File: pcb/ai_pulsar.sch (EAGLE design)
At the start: 24 parts, among them IC1 DS1307SO8-TIGHT, IC3 74HCT245MTC, J2 1X05, U1 MIC5205-3.3

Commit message: routing finished
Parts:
- 3V-BATT: value (none) -> CR1220
- D1: value (none) -> PMEG2010AEB; device Ai_DiscreteSemis:DIODE-SCHOTTKYSMA-403D -> Ai_DiscreteSemis:DIODE-SCHOTTKYSOD-523
- J1: value (none) -> JST-3-MALE
- XL1: value (none) -> CMR200T
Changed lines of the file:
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@@
 <part name="U$7" library="Ai_Power" deviceset="5V" device=""/>
 <part name="U$11" library="Ai_Power" deviceset="5V" device=""/>
-<part name="3V-BATT" library="Ai_Connectors" deviceset="CR1220" device="SMT"/>
+<part name="3V-BATT" library="Ai_Connectors" deviceset="CR1220" device="SMT" value="CR1220"/>
 <part name="IC1" library="Ai_IC" deviceset="DS1307" device="SO8-TIGHT"/>
-<part name="J1" library="Ai_Connectors" deviceset="JST-3-MALE" device=""/>
+<part name="J1" library="Ai_Connectors" deviceset="JST-3-MALE" device="" value=""/>
 <part name="-" library="Ai_Connectors" deviceset="1X01-PETAL" device=""/>
 <part name="+" library="Ai_Connectors" deviceset="1X01-PETAL" device=""/>
@@
 <part name="R3" library="Ai_Passives" deviceset="RES" device="0603" value="10K"/>
 <part name="U$2" library="Ai_Power" deviceset="5V" device=""/>
-<part name="XL1" library="Ai_FrequencyControl" deviceset="CRYSTAL" device="CYL-2X6MM-SMT"/>
+<part name="XL1" library="Ai_FrequencyControl" deviceset="CRYSTAL" device="CYL-2X6MM-SMT" value="CMR200T"/>
 <part name="U$3" library="Ai_Power" deviceset="3V3" device=""/>
-<part name="D1" library="Ai_DiscreteSemis" deviceset="DIODE-SCHOTTKY" device="SMA-403D"/>
+<part name="D1" library="Ai_DiscreteSemis" deviceset="DIODE-SCHOTTKY" device="SOD-523" value="PMEG2010AEB"/>
 </parts>
 <sheets>
@@
 </sheet>
 </sheets>
+<errors>
+</errors>
 </schematic>
 </drawing>

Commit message: renamed a few parts
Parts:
- C1: value 0.01uF -> 0.1uF
- renumbered IC3 to IC2
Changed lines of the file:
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@@
 <?xml version="1.0" encoding="utf-8"?>
 <!DOCTYPE eagle SYSTEM "eagle.dtd">
-<eagle version="7.1.0">
+<eagle version="7.0.0">
 <drawing>
 <settings>
@@
 <setting verticaltext="up"/>
 </settings>
-<grid distance="50" unitdist="mil" unit="mil" style="lines" multiple="1" display="yes" altdistance="0.01" altunitdist="inch" altunit="inch"/>
+<grid distance="0.1" unitdist="inch" unit="inch" style="lines" multiple="1" display="no" altdistance="0.01" altunitdist="inch" altunit="inch"/>
 <layers>
 <layer number="1" name="Top" color="4" fill="1" visible="no" active="no"/>
@@
 <part name="R1" library="Ai_Passives" deviceset="RES" device="0603" value="1K"/>
 <part name="R2" library="Ai_Passives" deviceset="RES" device="0603" value="1K"/>
-<part name="C1" library="Ai_Passives" deviceset="CAP" device="0603" value="0.01uF"/>
+<part name="C1" library="Ai_Passives" deviceset="CAP" device="0603" value="0.1uF"/>
 <part name="GND5" library="Ai_Power" deviceset="GND" device=""/>
 <part name="U$1" library="Ai_Power" deviceset="3V3" device=""/>
 <part name="GND4" library="Ai_Power" deviceset="GND" device=""/>
 <part name="GND8" library="Ai_Power" deviceset="GND" device=""/>
-<part name="IC3" library="Ai_IC" deviceset="74HCT245" device="MTC"/>
+<part name="IC2" library="Ai_IC" deviceset="74HCT245" device="MTC"/>
 <part name="GND11" library="Ai_Power" deviceset="GND" device=""/>
 <part name="U$10" library="Ai_Power" deviceset="5V" device=""/>
@@
 <instance part="GND4" gate="GND" x="106.68" y="123.19"/>
 <instance part="GND8" gate="GND" x="194.31" y="83.82"/>
-<instance part="IC3" gate="74HCT245" x="179.07" y="101.6"/>
+<instance part="IC2" gate="74HCT245" x="179.07" y="101.6"/>
 <instance part="GND11" gate="GND" x="181.61" y="50.8"/>
 <instance part="U$10" gate="G$1" x="180.34" y="63.5"/>
@@
 </segment>
 <segment>
-<pinref part="IC3" gate="74HCT245" pin="VCC"/>
+<pinref part="IC2" gate="74HCT245" pin="VCC"/>
 <wire x1="166.37" y1="114.3" x2="163.83" y2="114.3" width="0.1524" layer="91"/>
 <pinref part="U$7" gate="G$1" pin="5V"/>
 <wire x1="163.83" y1="114.3" x2="163.83" y2="116.84" width="0.1524" layer="91"/>
-<pinref part="IC3" gate="74HCT245" pin="DIR"/>
+<pinref part="IC2" gate="74HCT245" pin="DIR"/>
 <wire x1="166.37" y1="111.76" x2="163.83" y2="111.76" width="0.1524" layer="91"/>
 <wire x1="163.83" y1="111.76" x2="163.83" y2="114.3" width="0.1524" layer="91"/>
@@
 </segment>
 <segment>
-<pinref part="IC3" gate="74HCT245" pin="GND"/>
+<pinref part="IC2" gate="74HCT245" pin="GND"/>
 <wire x1="191.77" y1="88.9" x2="194.31" y2="88.9" width="0.1524" layer="91"/>
 <pinref part="GND8" gate="GND" pin="GND"/>
 <wire x1="194.31" y1="88.9" x2="194.31" y2="86.36" width="0.1524" layer="91"/>
-<pinref part="IC3" gate="74HCT245" pin="!OE"/>
+<pinref part="IC2" gate="74HCT245" pin="!OE"/>
 <wire x1="191.77" y1="91.44" x2="194.31" y2="91.44" width="0.1524" layer="91"/>
 <wire x1="194.31" y1="91.44" x2="194.31" y2="88.9" width="0.1524" layer="91"/>
@@
 </segment>
 <segment>
-<pinref part="IC3" gate="74HCT245" pin="A1"/>
+<pinref part="IC2" gate="74HCT245" pin="A1"/>
 <wire x1="166.37" y1="106.68" x2="163.83" y2="106.68" width="0.1524" layer="91"/>
 <label x="163.83" y="106.68" size="1.27" layer="95" font="vector" ratio="10" rot="R180" xref="yes"/>
@@
 <net name="5VIO2" class="0">
 <segment>
-<pinref part="IC3" gate="74HCT245" pin="B1"/>
+<pinref part="IC2" gate="74HCT245" pin="B1"/>
 <wire x1="191.77" y1="114.3" x2="194.31" y2="114.3" width="0.1524" layer="91"/>
 <label x="194.31" y="114.3" size="1.27" layer="95" font="vector" ratio="10" xref="yes"/>

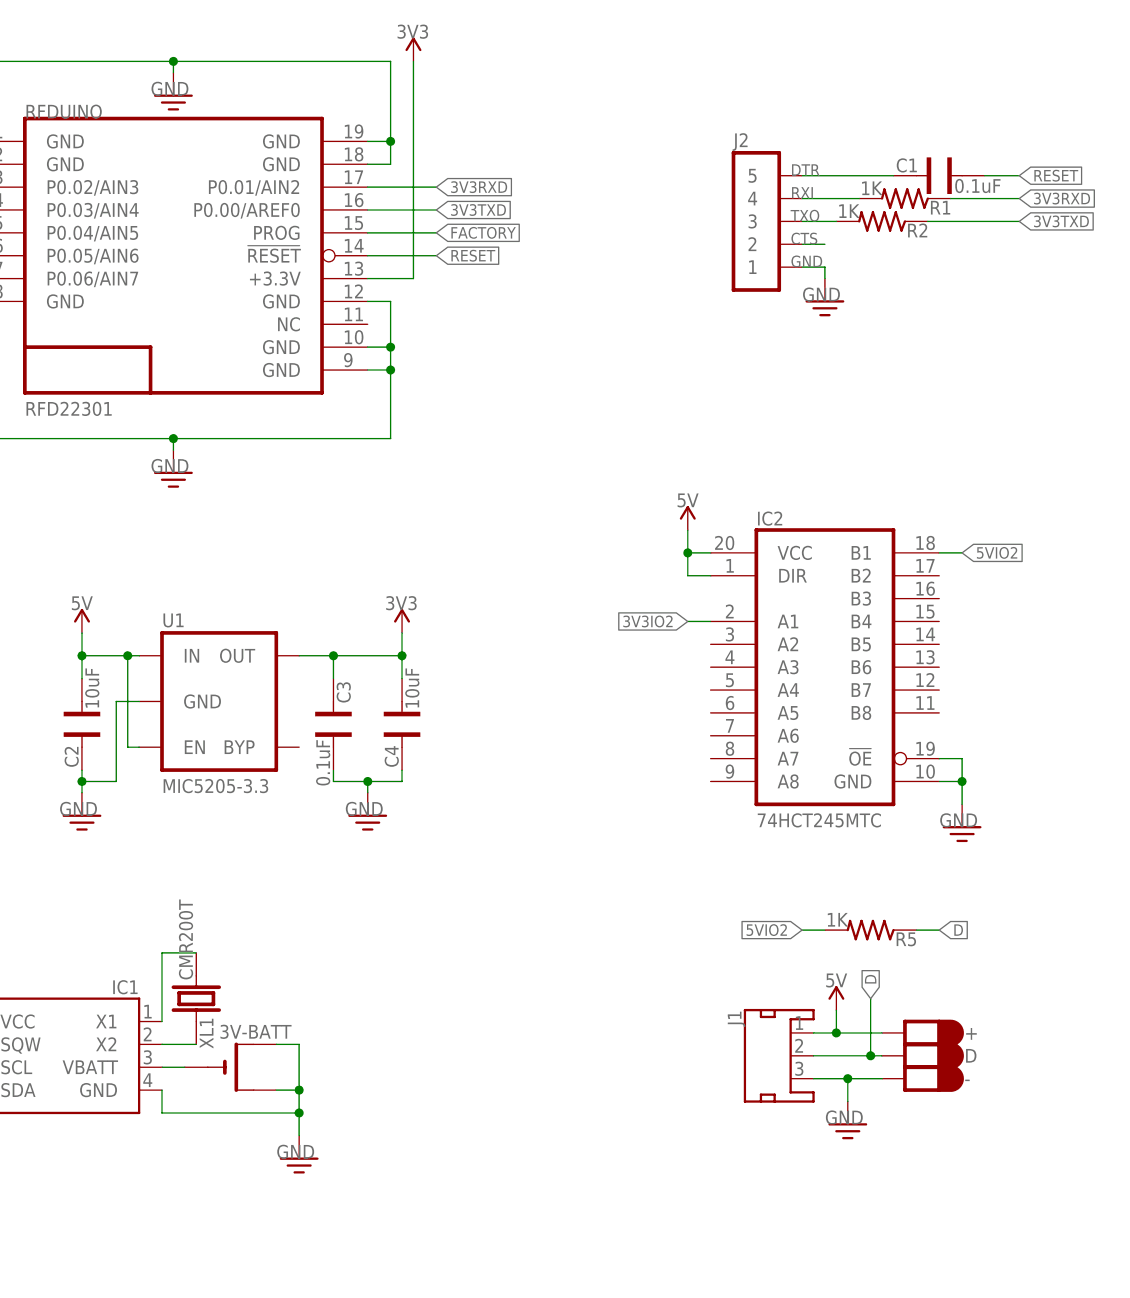
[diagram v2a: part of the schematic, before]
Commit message: version 1.1. Fixed coin-cell polarity, added 5V on FTDI pins for easy programming
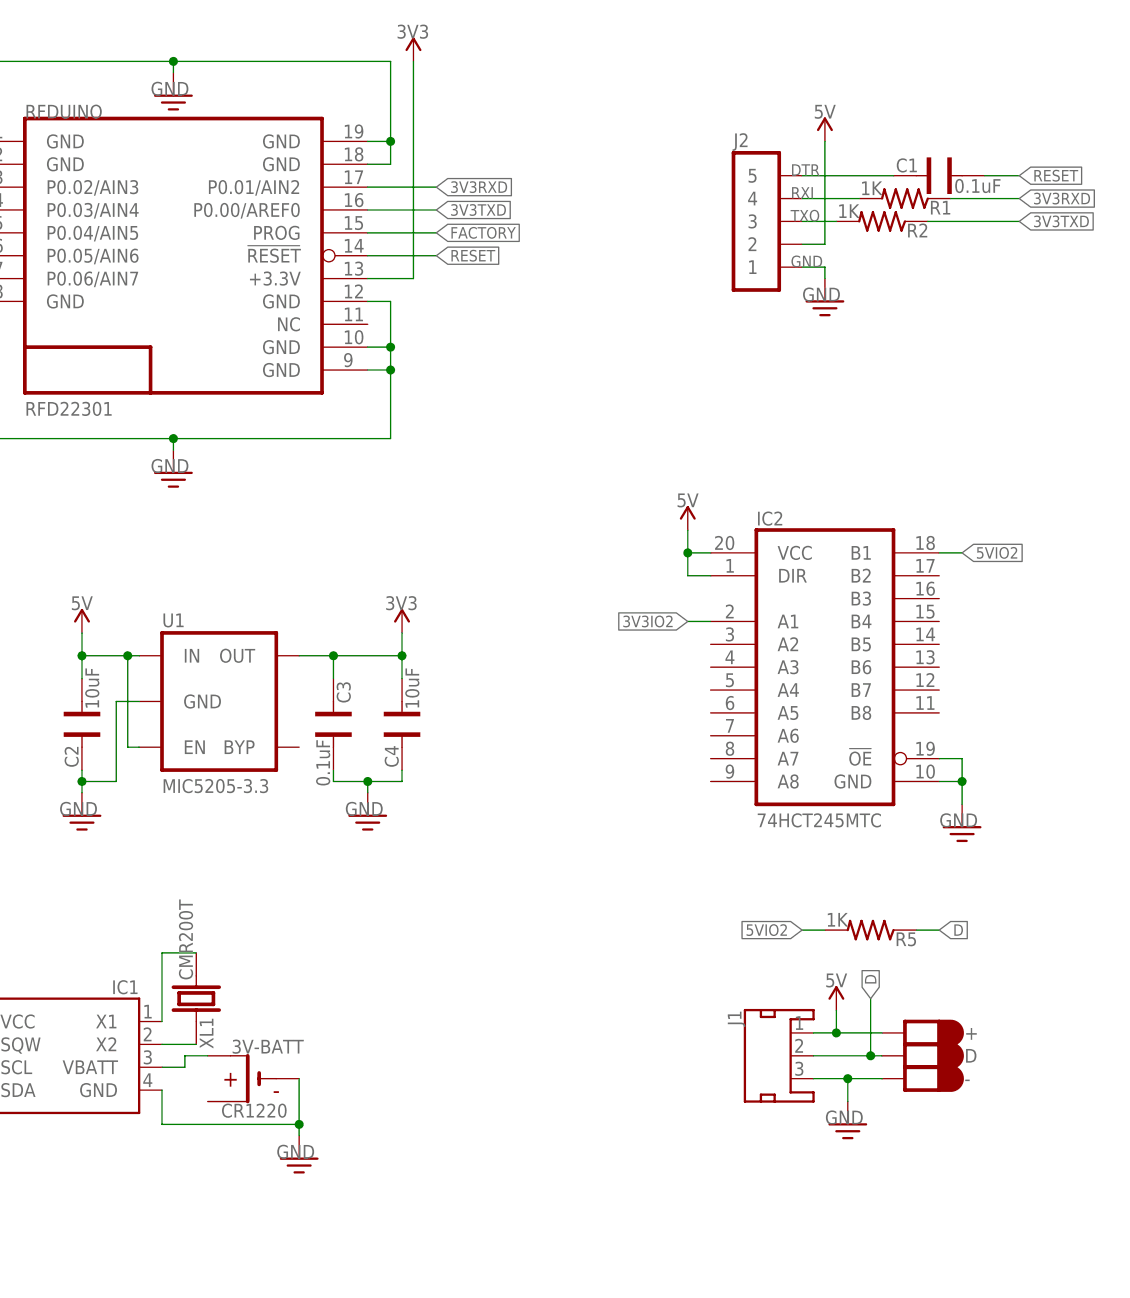
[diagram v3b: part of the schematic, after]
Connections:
- removed net CTS: J2.2
- removed net N$2: 3V-BATT.-, IC1.VBATT
- new net N$1: 3V-BATT.+1, IC1.VBATT
- net 5V: now also J2.2
- net GND: now also 3V-BATT.-; no longer 3V-BATT.+@1, 3V-BATT.+@2
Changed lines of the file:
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@@
 <?xml version="1.0" encoding="utf-8"?>
 <!DOCTYPE eagle SYSTEM "eagle.dtd">
-<eagle version="7.0.0">
+<eagle version="7.1.0">
 <drawing>
 <settings>
@@
 <setting verticaltext="up"/>
 </settings>
-<grid distance="0.1" unitdist="inch" unit="inch" style="lines" multiple="1" display="no" altdistance="0.01" altunitdist="inch" altunit="inch"/>
+<grid distance="50" unitdist="mil" unit="mil" style="lines" multiple="1" display="yes" altdistance="0.01" altunitdist="inch" altunit="inch"/>
 <layers>
 <layer number="1" name="Top" color="4" fill="1" visible="no" active="no"/>
@@
 <part name="FRAME1" library="Ai_Miscellany" deviceset="FRAME-LETTER" device="">
 <attribute name="AUTHOR" value="A.I. HARDWARE SITH LORDS"/>
-<attribute name="REV" value="1.2"/>
+<attribute name="REV" value="1.1"/>
 </part>
 <part name="C2" library="Ai_Passives" deviceset="CAP" device="0603" value="10uF"/>
@@
 <part name="U$7" library="Ai_Power" deviceset="5V" device=""/>
 <part name="U$11" library="Ai_Power" deviceset="5V" device=""/>
-<part name="3V-BATT" library="Ai_Connectors" deviceset="CR1220" device="SMT" value="CR1220"/>
 <part name="IC1" library="Ai_IC" deviceset="DS1307" device="SO8-TIGHT"/>
-<part name="J1" library="Ai_Connectors" deviceset="JST-3-MALE" device="" value=""/>
+<part name="J1" library="Ai_Connectors" deviceset="JST-3-MALE" device="" value="JST-3-MALE"/>
 <part name="-" library="Ai_Connectors" deviceset="1X01-PETAL" device=""/>
 <part name="+" library="Ai_Connectors" deviceset="1X01-PETAL" device=""/>
@@
 <part name="U$3" library="Ai_Power" deviceset="3V3" device=""/>
 <part name="D1" library="Ai_DiscreteSemis" deviceset="DIODE-SCHOTTKY" device="SOD-523" value="PMEG2010AEB"/>
+<part name="U$5" library="Ai_Power" deviceset="5V" device=""/>
+<part name="3V-BATT" library="Ai_Connectors" deviceset="CR1220" device="SMT" value="CR1220"/>
 </parts>
 <sheets>
@@
 <instance part="U$7" gate="G$1" x="163.83" y="116.84"/>
 <instance part="U$11" gate="G$1" x="67.31" y="105.41"/>
-<instance part="3V-BATT" gate="G$1" x="113.03" y="57.15"/>
 <instance part="IC1" gate="G$1" x="95.25" y="59.69" rot="MR0"/>
 <instance part="J1" gate="G$1" x="172.72" y="58.42" rot="MR270"/>
@@
 <instance part="U$3" gate="G$1" x="78.74" y="77.47"/>
 <instance part="D1" gate="G$1" x="62.23" y="102.87"/>
+<instance part="U$5" gate="G$1" x="179.07" y="160.02"/>
+<instance part="3V-BATT" gate="G$1" x="115.57" y="55.88" smashed="yes" rot="MR0">
+<attribute name="NAME" x="121.158" y="58.674" size="1.524" layer="95" font="vector" ratio="10" rot="MR0"/>
+<attribute name="VALUE" x="119.38" y="51.562" size="1.524" layer="96" font="vector" ratio="10" rot="MR0"/>
+</instance>
 </instances>
 <busses>
@@
 <wire x1="163.83" y1="111.76" x2="163.83" y2="114.3" width="0.1524" layer="91"/>
 <junction x="163.83" y="114.3"/>
+</segment>
+<segment>
+<pinref part="J2" gate="G$1" pin="2"/>
+<wire x1="176.53" y1="148.59" x2="179.07" y2="148.59" width="0.1524" layer="91"/>
+<wire x1="179.07" y1="148.59" x2="179.07" y2="160.02" width="0.1524" layer="91"/>
+<pinref part="U$5" gate="G$1" pin="5V"/>
 </segment>
 </net>
@@
 </segment>
 <segment>
-<pinref part="3V-BATT" gate="G$1" pin="+@1"/>
-<wire x1="118.11" y1="59.69" x2="120.65" y2="59.69" width="0.1524" layer="91"/>
-<wire x1="120.65" y1="59.69" x2="120.65" y2="54.61" width="0.1524" layer="91"/>
-<pinref part="3V-BATT" gate="G$1" pin="+@2"/>
-<wire x1="120.65" y1="54.61" x2="120.65" y2="52.07" width="0.1524" layer="91"/>
-<wire x1="120.65" y1="52.07" x2="120.65" y2="49.53" width="0.1524" layer="91"/>
-<wire x1="118.11" y1="54.61" x2="120.65" y2="54.61" width="0.1524" layer="91"/>
-<junction x="120.65" y="54.61"/>
+<wire x1="120.65" y1="55.88" x2="120.65" y2="50.8" width="0.1524" layer="91"/>
+<wire x1="120.65" y1="50.8" x2="120.65" y2="49.53" width="0.1524" layer="91"/>
 <pinref part="GND2" gate="GND" pin="GND"/>
 <pinref part="IC1" gate="G$1" pin="GND"/>
-<wire x1="120.65" y1="52.07" x2="105.41" y2="52.07" width="0.1524" layer="91"/>
-<wire x1="105.41" y1="52.07" x2="105.41" y2="54.61" width="0.1524" layer="91"/>
-<junction x="120.65" y="52.07"/>
+<wire x1="120.65" y1="50.8" x2="105.41" y2="50.8" width="0.1524" layer="91"/>
+<wire x1="105.41" y1="50.8" x2="105.41" y2="54.61" width="0.1524" layer="91"/>
+<junction x="120.65" y="50.8"/>
+<pinref part="3V-BATT" gate="G$1" pin="-"/>
 </segment>
 <segment>
@@
 </segment>
 </net>
-<net name="N$2" class="0">
-<segment>
-<pinref part="IC1" gate="G$1" pin="VBATT"/>
-<pinref part="3V-BATT" gate="G$1" pin="-"/>
-<wire x1="105.41" y1="57.15" x2="107.95" y2="57.15" width="0.1524" layer="91"/>
-</segment>
-</net>
-<net name="CTS" class="0">
-<segment>
-<pinref part="J2" gate="G$1" pin="2"/>
-<wire x1="176.53" y1="148.59" x2="179.07" y2="148.59" width="0.1524" layer="91"/>
-<label x="175.26" y="148.59" size="1.27" layer="95" font="vector" ratio="10"/>
-</segment>
-</net>
 <net name="TXO" class="0">
 <segment>
@@
 </segment>
 </net>
+<net name="N$1" class="0">
+<segment>
+<pinref part="IC1" gate="G$1" pin="VBATT"/>
+<wire x1="105.41" y1="57.15" x2="107.95" y2="57.15" width="0.1524" layer="91"/>
+<wire x1="107.95" y1="57.15" x2="107.95" y2="58.42" width="0.1524" layer="91"/>
+<wire x1="107.95" y1="58.42" x2="110.49" y2="58.42" width="0.1524" layer="91"/>
+<pinref part="3V-BATT" gate="G$1" pin="+1"/>
+</segment>
+</net>

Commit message: minor silkscreen fix
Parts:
- J1: value JST-3-MALE -> JST-3P-MALE; device Ai_Connectors:JST-3-MALE -> Ai_Connectors:JST-3P-MALE
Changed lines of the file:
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@@
 <part name="U$11" library="Ai_Power" deviceset="5V" device=""/>
 <part name="IC1" library="Ai_IC" deviceset="DS1307" device="SO8-TIGHT"/>
-<part name="J1" library="Ai_Connectors" deviceset="JST-3-MALE" device="" value="JST-3-MALE"/>
+<part name="J1" library="Ai_Connectors" deviceset="JST-3P-MALE" device="" value="JST-3P-MALE"/>
 <part name="-" library="Ai_Connectors" deviceset="1X01-PETAL" device=""/>
 <part name="+" library="Ai_Connectors" deviceset="1X01-PETAL" device=""/>

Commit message: Updating
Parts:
- added C5: 100uF, Ai_Passives:CAP-POLEIA3216
- D1: device Ai_DiscreteSemis:DIODE-SCHOTTKYSOD-523 -> Ai_DiscreteSemis:DIODE-SCHOTTKYSMA-403D
- U1: value MIC5205-3.3 -> MIC5219-3.3; device Ai_Power:MIC5205-3.3 -> Ai_Power:MIC5219-3.3
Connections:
- net 5V: now also C5.A
- net GND: now also C5.C
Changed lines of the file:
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@@
 <layer number="56" name="wert" color="7" fill="1" visible="no" active="no"/>
 <layer number="57" name="tCAD" color="7" fill="1" visible="no" active="no"/>
+<layer number="90" name="Modules" color="5" fill="1" visible="no" active="no"/>
 <layer number="91" name="Nets" color="2" fill="1" visible="yes" active="yes"/>
 <layer number="92" name="Busses" color="1" fill="1" visible="yes" active="yes"/>
@@
 <part name="FRAME1" library="Ai_Miscellany" deviceset="FRAME-LETTER" device="">
 <attribute name="AUTHOR" value="A.I. HARDWARE SITH LORDS"/>
-<attribute name="REV" value="1.1"/>
+<attribute name="REV" value="1.2"/>
 </part>
 <part name="C2" library="Ai_Passives" deviceset="CAP" device="0603" value="10uF"/>
@@
 <part name="+" library="Ai_Connectors" deviceset="1X01-PETAL" device=""/>
 <part name="D" library="Ai_Connectors" deviceset="1X01-PETAL" device=""/>
-<part name="U1" library="Ai_Power" deviceset="MIC5205-*" device="" technology="3.3"/>
+<part name="U1" library="Ai_Power" deviceset="MIC5219-*" device="" technology="3.3"/>
 <part name="J2" library="Ai_Connectors" deviceset="1X05" device=""/>
 <part name="GND2" library="Ai_Power" deviceset="GND" device=""/>
@@
 <part name="XL1" library="Ai_FrequencyControl" deviceset="CRYSTAL" device="CYL-2X6MM-SMT" value="CMR200T"/>
 <part name="U$3" library="Ai_Power" deviceset="3V3" device=""/>
-<part name="D1" library="Ai_DiscreteSemis" deviceset="DIODE-SCHOTTKY" device="SOD-523" value="PMEG2010AEB"/>
+<part name="D1" library="Ai_DiscreteSemis" deviceset="DIODE-SCHOTTKY" device="SMA-403D" value="PMEG2010AEB"/>
 <part name="U$5" library="Ai_Power" deviceset="5V" device=""/>
 <part name="3V-BATT" library="Ai_Connectors" deviceset="CR1220" device="SMT" value="CR1220"/>
+<part name="C5" library="Ai_Passives" deviceset="CAP-POL" device="EIA3216" value="100uF"/>
 </parts>
 <sheets>
@@
 <instance part="U$6" gate="G$1" x="139.7" y="15.24"/>
 <instance part="RFDUINO" gate="G$1" x="106.68" y="147.32"/>
-<instance part="GND1" gate="GND" x="59.69" y="90.17"/>
+<instance part="GND1" gate="GND" x="59.69" y="82.55"/>
 <instance part="R1" gate="G$1" x="187.96" y="153.67" rot="R180"/>
 <instance part="R2" gate="G$1" x="185.42" y="151.13" rot="R180"/>
@@
 <attribute name="VALUE" x="119.38" y="51.562" size="1.524" layer="96" font="vector" ratio="10" rot="MR0"/>
 </instance>
+<instance part="C5" gate="G$1" x="67.31" y="93.98" smashed="yes">
+<attribute name="NAME" x="66.929" y="89.408" size="1.524" layer="95" font="vector" ratio="10" rot="R90"/>
+<attribute name="VALUE" x="70.358" y="97.409" size="1.524" layer="96" font="vector" ratio="10" rot="R270"/>
+</instance>
 </instances>
 <busses>
@@
 <pinref part="D1" gate="G$1" pin="C"/>
 <wire x1="64.77" y1="102.87" x2="67.31" y2="102.87" width="0.1524" layer="91"/>
+<pinref part="C5" gate="G$1" pin="A"/>
+<wire x1="67.31" y1="99.06" x2="67.31" y2="102.87" width="0.1524" layer="91"/>
+<junction x="67.31" y="102.87"/>
 </segment>
 <segment>
@@
 <wire x1="57.15" y1="95.25" x2="59.69" y2="95.25" width="0.1524" layer="91"/>
 <pinref part="GND1" gate="GND" pin="GND"/>
-<wire x1="59.69" y1="95.25" x2="59.69" y2="92.71" width="0.1524" layer="91"/>
-</segment>
-<segment>
+<wire x1="59.69" y1="95.25" x2="59.69" y2="86.36" width="0.1524" layer="91"/>
+<pinref part="C5" gate="G$1" pin="C"/>
+<wire x1="59.69" y1="86.36" x2="59.69" y2="85.09" width="0.1524" layer="91"/>
+<wire x1="59.69" y1="86.36" x2="67.31" y2="86.36" width="0.1524" layer="91"/>
+<wire x1="67.31" y1="86.36" x2="67.31" y2="88.9" width="0.1524" layer="91"/>
+<junction x="59.69" y="86.36"/>
+</segment>
+<segment>
